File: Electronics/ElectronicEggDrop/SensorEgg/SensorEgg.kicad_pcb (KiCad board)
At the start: 2 copper layers, 52.9 x 74.6 mm, 4 parts, among them J1 Conn_01x06, J2 Conn_01x06, U1 LIS3DH, U2 SDCardReader

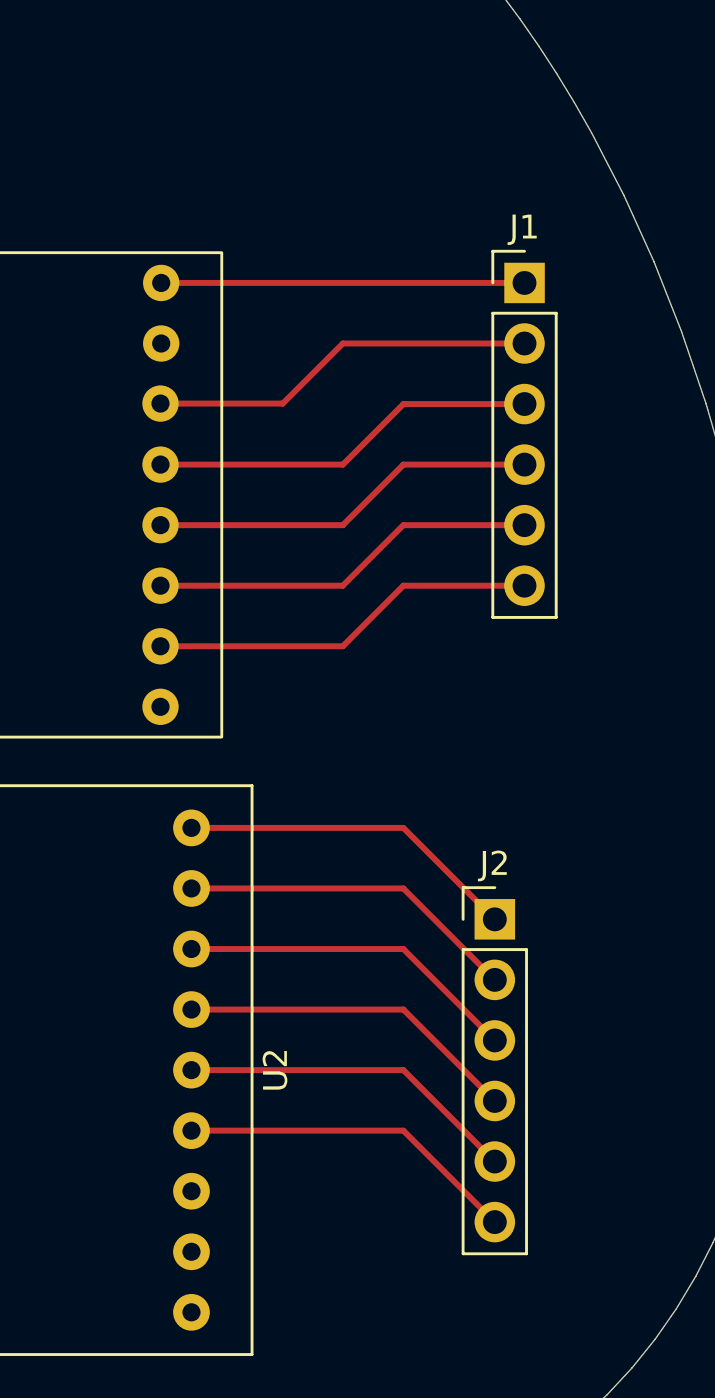
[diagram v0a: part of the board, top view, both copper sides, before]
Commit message: Started Assembly of boards, added Arduino nano and LIS3dh Boards, found new footprints for LIS3DH and SDreader, need to implement them.
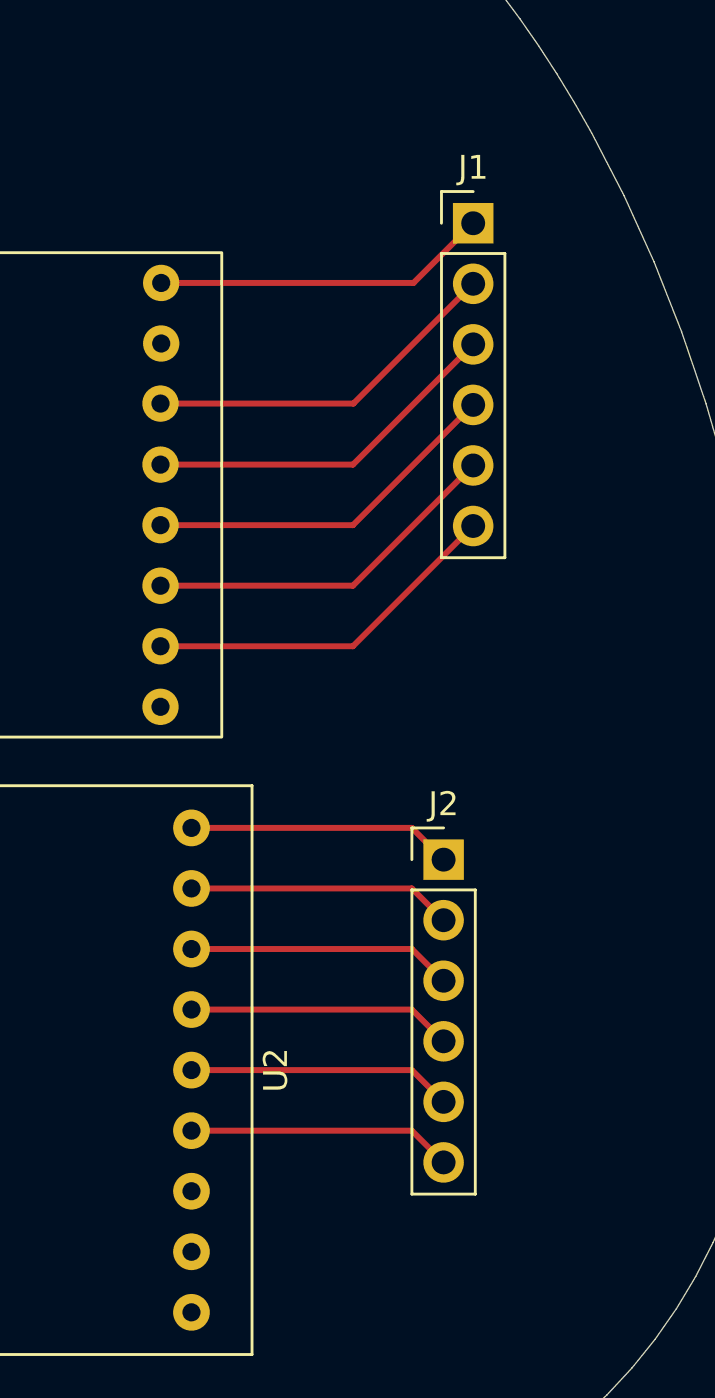
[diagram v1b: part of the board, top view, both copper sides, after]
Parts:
- moved J1 3.30 mm to (119.8, 83.9)
- moved J2 3.30 mm to (118.5, 110.6)
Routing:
- net Net-(J2-Pad5): track 14.3 -> 11.1 mm
- net Net-(J2-Pad3): track 14.3 -> 11.1 mm
- net Net-(J2-Pad1): track 14.3 -> 11.1 mm
- net Net-(J2-Pad6): track 14.3 -> 11.1 mm
- net Net-(J2-Pad4): track 14.3 -> 11.1 mm
- net Net-(J2-Pad2): track 14.3 -> 11.1 mm
- net Net-(J1-Pad1): track 15.2 -> 14.1 mm
- net Net-(J1-Pad6): track 16.3 -> 15.2 mm
- net Net-(J1-Pad5): track 16.3 -> 15.2 mm
- net Net-(J1-Pad4): track 16.3 -> 15.2 mm
- net Net-(J1-Pad3): track 16.3 -> 15.2 mm
- net Net-(J1-Pad2): track 16.3 -> 15.2 mm
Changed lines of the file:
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@@
   (net 20 "unconnected-(U2-Pad9)")
   (footprint "Connector_PinHeader_2.54mm:PinHeader_1x06_P2.54mm_Vertical" (layer "F.Cu")
-    (at 121.92 86.36)
+    (at 119.767007 83.855834)
     (descr "Through hole straight pin header, 1x06, 2.54mm pitch, single row")
     (tags "Through hole pin header THT 1x06 2.54mm single row")
@@
   )
   (footprint "Connector_PinHeader_2.54mm:PinHeader_1x06_P2.54mm_Vertical" (layer "F.Cu")
-    (at 120.675 113.055)
+    (at 118.525613 110.551233)
     (descr "Through hole straight pin header, 1x06, 2.54mm pitch, single row")
     (tags "Through hole pin header THT 1x06 2.54mm single row")
@@
     (effects (font (size 1.5 1.5) (thickness 0.3)))
   )
-  (segment (start 106.68 86.36) (end 121.92 86.36) (width 0.25) (layer "F.Cu") (net 1))
-  (segment (start 114.3 88.9) (end 121.92 88.9) (width 0.25) (layer "F.Cu") (net 2))
-  (segment (start 106.65025 91.4201) (end 111.7799 91.4201) (width 0.25) (layer "F.Cu") (net 2))
-  (segment (start 111.7799 91.4201) (end 114.3 88.9) (width 0.25) (layer "F.Cu") (net 2))
-  (segment (start 106.65025 93.98) (end 114.3 93.98) (width 0.25) (layer "F.Cu") (net 3))
-  (segment (start 114.3 93.98) (end 116.84 91.44) (width 0.25) (layer "F.Cu") (net 3))
-  (segment (start 116.84 91.44) (end 121.92 91.44) (width 0.25) (layer "F.Cu") (net 3))
-  (segment (start 116.84 93.98) (end 121.92 93.98) (width 0.25) (layer "F.Cu") (net 4))
-  (segment (start 114.3 96.52) (end 116.84 93.98) (width 0.25) (layer "F.Cu") (net 4))
-  (segment (start 106.65025 96.52) (end 114.3 96.52) (width 0.25) (layer "F.Cu") (net 4))
-  (segment (start 106.65025 99.06) (end 114.3 99.06) (width 0.25) (layer "F.Cu") (net 5))
-  (segment (start 114.3 99.06) (end 116.84 96.52) (width 0.25) (layer "F.Cu") (net 5))
-  (segment (start 116.84 96.52) (end 121.92 96.52) (width 0.25) (layer "F.Cu") (net 5))
-  (segment (start 116.84 99.06) (end 121.92 99.06) (width 0.25) (layer "F.Cu") (net 6))
-  (segment (start 106.65025 101.6) (end 114.3 101.6) (width 0.25) (layer "F.Cu") (net 6))
-  (segment (start 114.3 101.6) (end 116.84 99.06) (width 0.25) (layer "F.Cu") (net 6))
-  (segment (start 116.84 109.22) (end 120.675 113.055) (width 0.25) (layer "F.Cu") (net 7))
-  (segment (start 107.95 109.22) (end 116.84 109.22) (width 0.25) (layer "F.Cu") (net 7))
-  (segment (start 116.84 111.76) (end 120.675 115.595) (width 0.25) (layer "F.Cu") (net 8))
-  (segment (start 107.95 111.76) (end 116.84 111.76) (width 0.25) (layer "F.Cu") (net 8))
-  (segment (start 116.84 114.3) (end 120.675 118.135) (width 0.25) (layer "F.Cu") (net 9))
-  (segment (start 107.95 114.3) (end 116.84 114.3) (width 0.25) (layer "F.Cu") (net 9))
-  (segment (start 116.84 116.84) (end 120.675 120.675) (width 0.25) (layer "F.Cu") (net 10))
-  (segment (start 107.95 116.84) (end 116.84 116.84) (width 0.25) (layer "F.Cu") (net 10))
-  (segment (start 107.95 119.38) (end 116.84 119.38) (width 0.25) (layer "F.Cu") (net 11))
-  (segment (start 116.84 119.38) (end 120.675 123.215) (width 0.25) (layer "F.Cu") (net 11))
-  (segment (start 116.84 121.92) (end 120.675 125.755) (width 0.25) (layer "F.Cu") (net 12))
-  (segment (start 107.95 121.92) (end 116.84 121.92) (width 0.25) (layer "F.Cu") (net 12))
+  (segment (start 117.262841 86.36) (end 119.767007 83.855834) (width 0.25) (layer "F.Cu") (net 1))
+  (segment (start 106.68 86.36) (end 117.262841 86.36) (width 0.25) (layer "F.Cu") (net 1))
+  (segment (start 106.65025 91.4201) (end 114.742741 91.4201) (width 0.25) (layer "F.Cu") (net 2))
+  (segment (start 114.742741 91.4201) (end 119.767007 86.395834) (width 0.25) (layer "F.Cu") (net 2))
+  (segment (start 114.722841 93.98) (end 119.767007 88.935834) (width 0.25) (layer "F.Cu") (net 3))
+  (segment (start 106.65025 93.98) (end 114.722841 93.98) (width 0.25) (layer "F.Cu") (net 3))
+  (segment (start 114.722841 96.52) (end 119.767007 91.475834) (width 0.25) (layer "F.Cu") (net 4))
+  (segment (start 106.65025 96.52) (end 114.722841 96.52) (width 0.25) (layer "F.Cu") (net 4))
+  (segment (start 114.722841 99.06) (end 119.767007 94.015834) (width 0.25) (layer "F.Cu") (net 5))
+  (segment (start 106.65025 99.06) (end 114.722841 99.06) (width 0.25) (layer "F.Cu") (net 5))
+  (segment (start 114.722841 101.6) (end 119.767007 96.555834) (width 0.25) (layer "F.Cu") (net 6))
+  (segment (start 106.65025 101.6) (end 114.722841 101.6) (width 0.25) (layer "F.Cu") (net 6))
+  (segment (start 117.19438 109.22) (end 118.525613 110.551233) (width 0.25) (layer "F.Cu") (net 7))
+  (segment (start 107.95 109.22) (end 117.19438 109.22) (width 0.25) (layer "F.Cu") (net 7))
+  (segment (start 117.19438 111.76) (end 118.525613 113.091233) (width 0.25) (layer "F.Cu") (net 8))
+  (segment (start 107.95 111.76) (end 117.19438 111.76) (width 0.25) (layer "F.Cu") (net 8))
+  (segment (start 107.95 114.3) (end 117.19438 114.3) (width 0.25) (layer "F.Cu") (net 9))
+  (segment (start 117.19438 114.3) (end 118.525613 115.631233) (width 0.25) (layer "F.Cu") (net 9))
+  (segment (start 107.95 116.84) (end 117.19438 116.84) (width 0.25) (layer "F.Cu") (net 10))
+  (segment (start 117.19438 116.84) (end 118.525613 118.171233) (width 0.25) (layer "F.Cu") (net 10))
+  (segment (start 117.19438 119.38) (end 118.525613 120.711233) (width 0.25) (layer "F.Cu") (net 11))
+  (segment (start 107.95 119.38) (end 117.19438 119.38) (width 0.25) (layer "F.Cu") (net 11))
+  (segment (start 107.95 121.92) (end 117.19438 121.92) (width 0.25) (layer "F.Cu") (net 12))
+  (segment (start 117.19438 121.92) (end 118.525613 123.251233) (width 0.25) (layer "F.Cu") (net 12))
   (group "" (id 753dc3a0-76f0-47fb-ae11-265f011cf233)
     (members

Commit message: Finished the PCBs
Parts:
- added ?: , , F.Cu at (89.3, 127.0)
- added M2: MountingHole_2.2mm_M2_DIN965_Pad, MountingHole:MountingHole_2.2mm_M2_DIN965_Pad, F.Cu at (89.3, 127.0)
- added M2: MountingHole_2.2mm_M2_DIN965_Pad, MountingHole:MountingHole_2.2mm_M2_DIN965_Pad, F.Cu at (89.3, 86.4)
- LIS3DH Connector: renamed from J1
- SD Card Reader Connector: renamed from J2
- U1, U2: moved to B.Cu
- moved U2 15.0 mm to (94.3, 119.4)
- moved U1 5.68 mm to (104.1, 78.7), turned to 180 degrees
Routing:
- net Net-(J2-Pad4): track 11.1 -> 24.8 mm
- net Net-(J2-Pad3): track 11.1 -> 24.8 mm
- net Net-(J2-Pad5): track 11.1 -> 24.8 mm
- net Net-(J2-Pad2): track 11.1 -> 24.8 mm
- net Net-(J2-Pad1): track 11.1 -> 24.8 mm
- net Net-(J2-Pad6): track 11.1 -> 23.6 mm
- net Net-(J1-Pad1): track 14.1 -> 23.3 mm
- net Net-(J1-Pad6): track 15.2 -> 24.3 mm
- net Net-(J1-Pad4): track 15.2 -> 24.3 mm
- net Net-(J1-Pad2): track 15.2 -> 24.2 mm
- net Net-(J1-Pad5): track 15.2 -> 24.3 mm
- net Net-(J1-Pad3): track 15.2 -> 24.3 mm
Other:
- board text added: "To get to the other Side!"
- board text added: "Why did the chicken cross the road?"

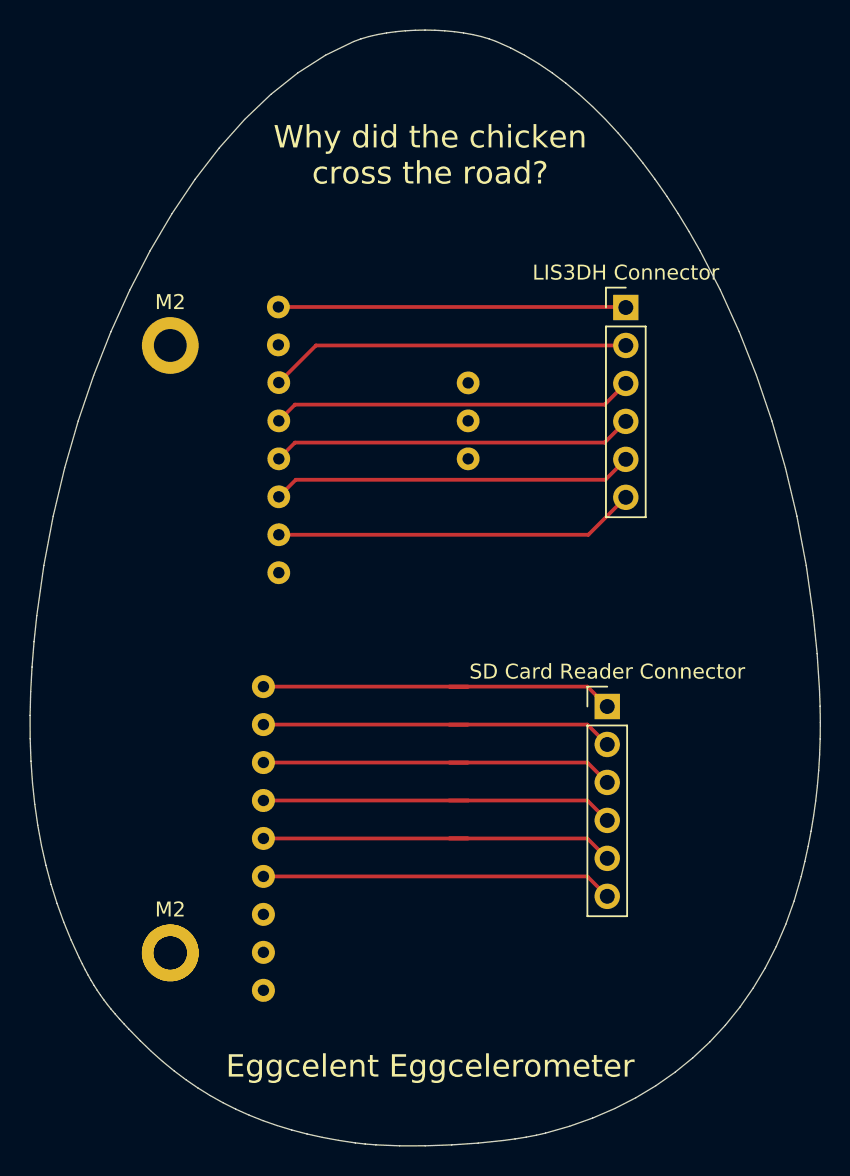
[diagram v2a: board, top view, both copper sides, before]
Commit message: Finished V1 of boards, sent them out for manufacturing, BOM genereated but needs editing.
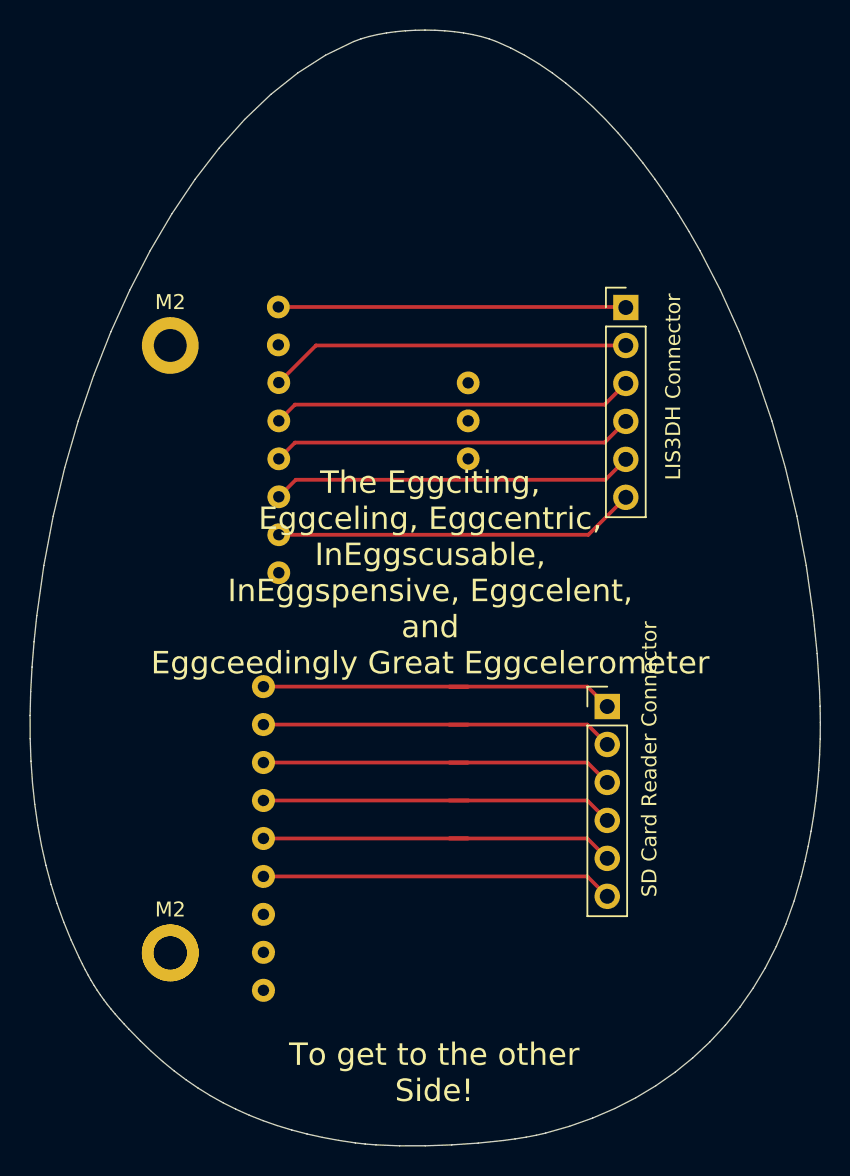
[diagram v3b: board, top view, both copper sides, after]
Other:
- board text added: "The Eggciting, Eggceling, Eggcentric, InEggscusable, InEggspensive, Eggcelent, and Eggceedingly Great Eggcelerometer"
- board text removed: "Eggcelent Eggcelerometer"
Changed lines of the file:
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@@
       (outputformat 1)
       (mirror false)
-      (drillshape 1)
+      (drillshape 0)
       (scaleselection 1)
-      (outputdirectory "")
+      (outputdirectory "../../GerberFiles/SensorEgg/")
     )
   )
@@
     (property "Sheetname" "")
     (attr through_hole)
-    (fp_text reference "LIS3DH Connector" (at 0 -2.33) (layer "F.SilkS")
+    (fp_text reference "LIS3DH Connector" (at 3.170293 5.309171 270) (layer "F.SilkS")
       (effects (font (size 1 1) (thickness 0.15)))
     )
@@
     (property "Sheetname" "")
     (attr through_hole)
-    (fp_text reference "SD Card Reader Connector" (at 0 -2.33) (layer "F.SilkS")
+    (fp_text reference "SD Card Reader Connector" (at 2.821652 3.524316 270) (layer "F.SilkS")
       (effects (font (size 1 1) (thickness 0.15)))
     )
@@
       (effects (font (size 1 1) (thickness 0.15)) (justify mirror))
     )
-    (fp_text value "LIS3DH" (at 0 1.27 unlocked) (layer "B.Fab")
+    (fp_text value "LIS3DH" (at -0.2725 -60.11359 unlocked) (layer "B.Fab")
       (effects (font (size 1 1) (thickness 0.15)) (justify mirror))
     )
@@
   (gr_line (start 111.573464 139.587767) (end 109.890768 139.761215) (layer "Edge.Cuts") (width 0.025399))
   (gr_line (start 90.329829 135.518508) (end 89.544514 134.92888) (layer "Edge.Cuts") (width 0.025399))
-  (gr_text "To get to the other\nSide!" (at 106.68 73.66) (layer "B.SilkS")
+  (gr_text "Why did the chicken\ncross the road?" (at 106.9525 135.04359) (layer "B.SilkS")
     (effects (font (size 1.5 1.5) (thickness 0.3)) (justify mirror))
   )
-  (gr_text "Why did the chicken\ncross the road?" (at 106.68 73.66) (layer "F.SilkS")
+  (gr_text "To get to the other\nSide!" (at 106.9525 135.04359) (layer "F.SilkS")
     (effects (font (size 1.5 1.5) (thickness 0.3)))
   )
-  (gr_text "Eggcelent Eggcelerometer" (at 106.68 134.62) (layer "F.SilkS")
+  (gr_text "The Eggciting, \nEggceling, Eggcentric, \nInEggscusable, \nInEggspensive, Eggcelent,\nand \nEggceedingly Great Eggcelerometer" (at 106.68 101.6) (layer "F.SilkS")
     (effects (font (size 1.5 1.5) (thickness 0.3)))
   )
